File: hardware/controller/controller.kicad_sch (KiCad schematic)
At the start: 0 parts

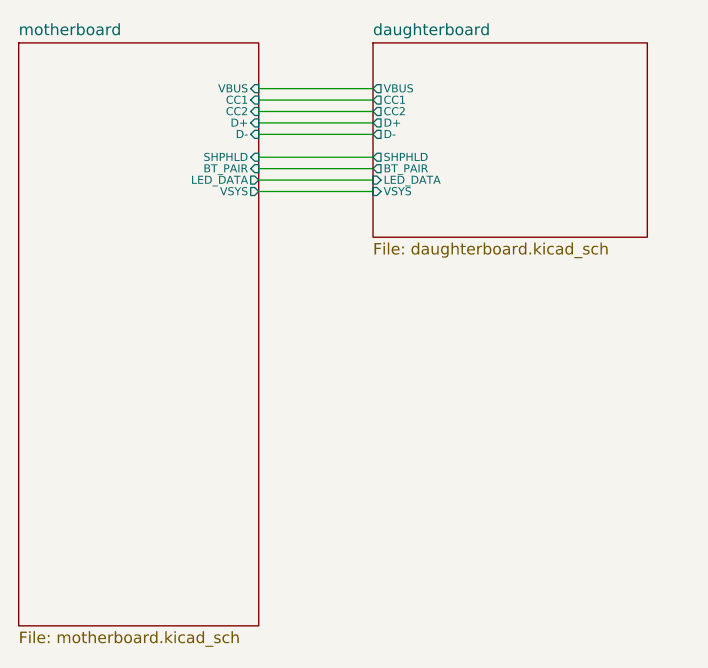
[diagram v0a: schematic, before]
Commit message: feat(controller): 1x10 MB-DB header, isolate DB nets, drop DB buttons and LEDs
J9 (MB) and J8 (DB) as Conn_01x10 with I1 pinout; DB nets renamed DB_*,
no hierarchical links between MB and DB sheets; SW89, SW91, D4, D92 removed.
Layout around J9 still to be tidied.

Co-Authored-By: Claude Opus 5.5 (1M context) <noreply@anthropic.com>
Claude-Session: https://claude.ai/code/session_011u4PgyeeXFvTvHcxLBDiHw
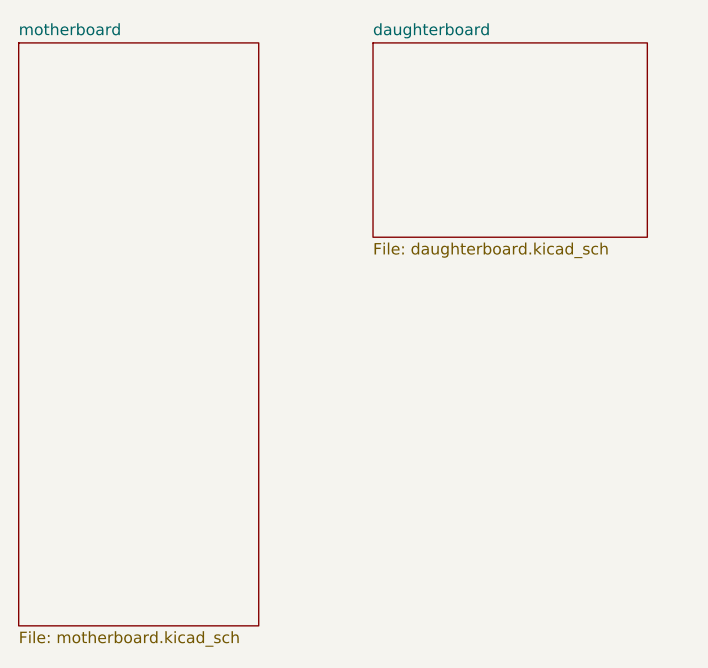
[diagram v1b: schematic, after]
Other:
- sheet daughterboard ports: added none; removed BT_PAIR, CC1, CC2, D+, D-, LED_DATA, SHPHLD, VBUS, VSYS
- sheet motherboard ports: added none; removed BT_PAIR, CC1, CC2, D+, D-, LED_DATA, SHPHLD, VBUS, VSYS
